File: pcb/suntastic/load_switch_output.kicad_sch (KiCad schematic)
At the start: 10 parts, among them J1 Screw_Terminal_01x02, U10 TC7WH08FK_LJCT, U6 TPS22917DBV

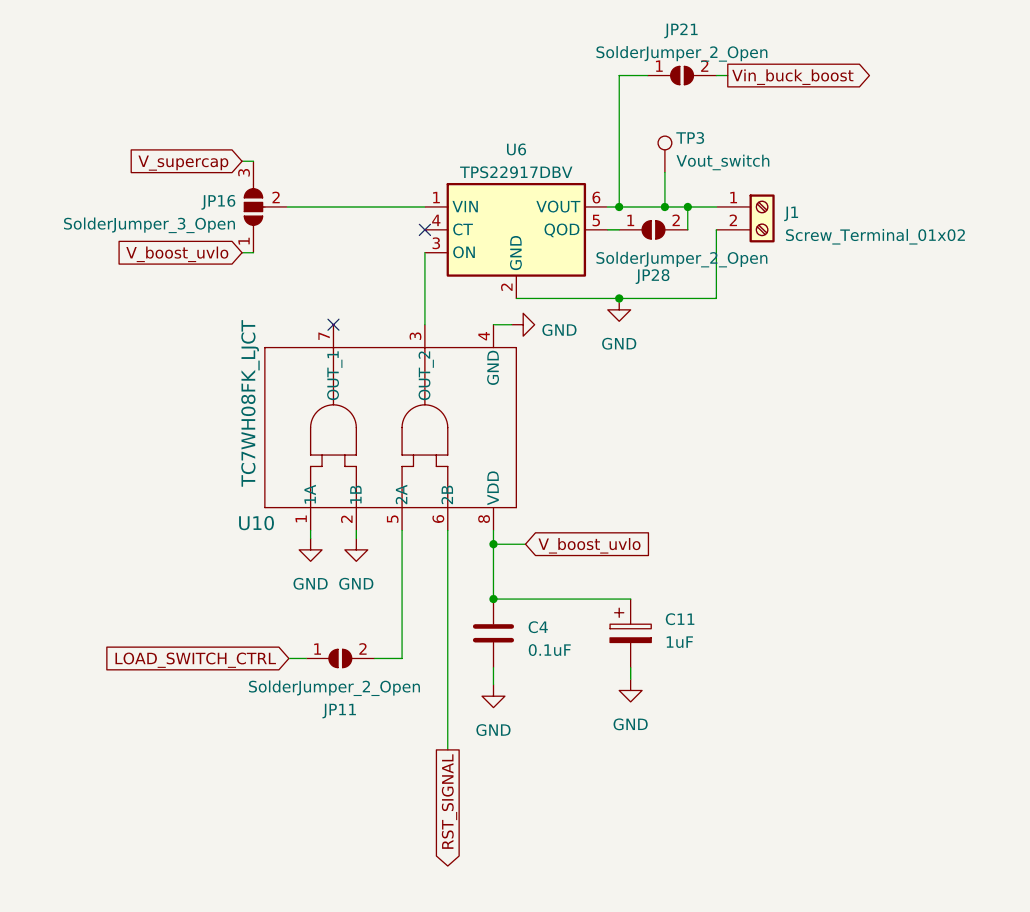
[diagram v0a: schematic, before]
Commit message: Add screw terminals for external MPPT module and PV input
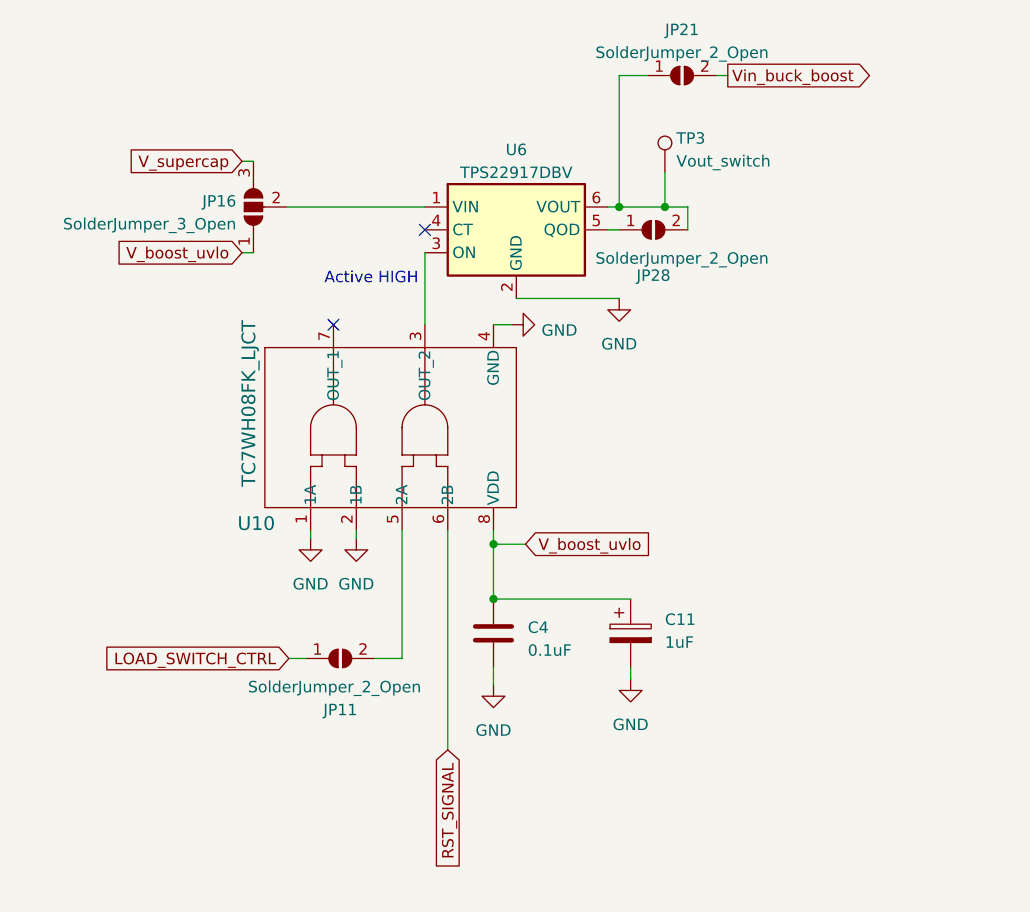
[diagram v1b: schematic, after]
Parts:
- removed J1: Screw_Terminal_01x02, TerminalBlock:TerminalBlock_bornier-2_P5.08mm, symbol Connector:Screw_Terminal_01x02
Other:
- note added: "Active HIGH"
